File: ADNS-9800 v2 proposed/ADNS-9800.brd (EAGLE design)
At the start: 32.7 x 32.5 mm, 27 parts, among them Q1 TRANSISTOR_SC-75

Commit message: V2 Design
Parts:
- R1, R2, R4: value (none) -> 1.8K
- R3, R5, R6: value (none) -> 3.3K
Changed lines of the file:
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@@
 <element name="SJ1" library="SparkFun-Passives" package="SJ_2S-TRACE" value="SOLDERJUMPERTRACE" x="5.2" y="21.52" smashed="yes" rot="MR180"/>
 <element name="SJ4" library="SparkFun-Passives" package="SJ_2S-NO" value="SOLDERJUMPERNO" x="5.2" y="11.12" smashed="yes" rot="MR0"/>
-<element name="R1" library="SparkFun-Passives" package="0603-RES" value="" x="5.1933" y="21.479" smashed="yes">
+<element name="R1" library="SparkFun-Passives" package="0603-RES" value="1.8K" x="5.1933" y="21.479" smashed="yes">
 <attribute name="NAME" x="4.6243" y="22.081" size="1.016" layer="25" font="vector" ratio="10"/>
-<attribute name="VALUE" x="4.1773" y="20.336" size="0.4064" layer="27" font="vector"/>
 </element>
-<element name="R6" library="SparkFun-Passives" package="0603-RES" value="" x="5.2" y="11.12" smashed="yes">
+<element name="R6" library="SparkFun-Passives" package="0603-RES" value="3.3K" x="5.2" y="11.12" smashed="yes">
 <attribute name="NAME" x="4.311" y="11.802" size="1.016" layer="25" font="vector" ratio="10"/>
-<attribute name="VALUE" x="4.184" y="9.977" size="0.4064" layer="27" font="vector"/>
 </element>
-<element name="R2" library="SparkFun-Passives" package="0603-RES" value="" x="5.2" y="23.84" smashed="yes">
+<element name="R2" library="SparkFun-Passives" package="0603-RES" value="1.8K" x="5.2" y="23.84" smashed="yes">
 <attribute name="NAME" x="4.631" y="24.442" size="1.016" layer="25" font="vector" ratio="10"/>
-<attribute name="VALUE" x="4.184" y="22.697" size="0.4064" layer="27" font="vector"/>
 </element>
 <element name="SJ2" library="SparkFun-Passives" package="SJ_2S-NO" value="SOLDERJUMPERNO" x="5.2" y="13.52" smashed="yes" rot="MR0"/>
-<element name="R3" library="SparkFun-Passives" package="0603-RES" value="" x="5.2" y="13.52" smashed="yes">
+<element name="R3" library="SparkFun-Passives" package="0603-RES" value="3.3K" x="5.2" y="13.52" smashed="yes">
 <attribute name="NAME" x="4.311" y="14.122" size="1.016" layer="25" font="vector" ratio="10"/>
-<attribute name="VALUE" x="4.184" y="12.377" size="0.4064" layer="27" font="vector"/>
 </element>
 <element name="SJ3" library="SparkFun-Passives" package="SJ_2S-TRACE" value="SOLDERJUMPERTRACE" x="5.12" y="23.84" smashed="yes" rot="MR180"/>
-<element name="R4" library="SparkFun-Passives" package="0603-RES" value="" x="5.2" y="19.12" smashed="yes">
+<element name="R4" library="SparkFun-Passives" package="0603-RES" value="1.8K" x="5.2" y="19.12" smashed="yes">
 <attribute name="NAME" x="4.631" y="19.722" size="1.016" layer="25" font="vector" ratio="10"/>
-<attribute name="VALUE" x="4.184" y="17.977" size="0.4064" layer="27" font="vector"/>
 </element>
 <element name="SJ5" library="SparkFun-Passives" package="SJ_2S-NO" value="SOLDERJUMPERNO" x="5.2" y="8.72" smashed="yes" rot="MR0"/>
-<element name="R5" library="SparkFun-Passives" package="0603-RES" value="" x="5.2" y="8.72" smashed="yes">
+<element name="R5" library="SparkFun-Passives" package="0603-RES" value="3.3K" x="5.2" y="8.72" smashed="yes">
 <attribute name="NAME" x="4.311" y="9.402" size="1.016" layer="25" font="vector" ratio="10"/>
-<attribute name="VALUE" x="4.184" y="7.577" size="0.4064" layer="27" font="vector"/>
 </element>
 <element name="SJ6" library="SparkFun-Passives" package="SJ_2S-TRACE" value="SOLDERJUMPERTRACE" x="5.2" y="19.12" smashed="yes" rot="MR180"/>

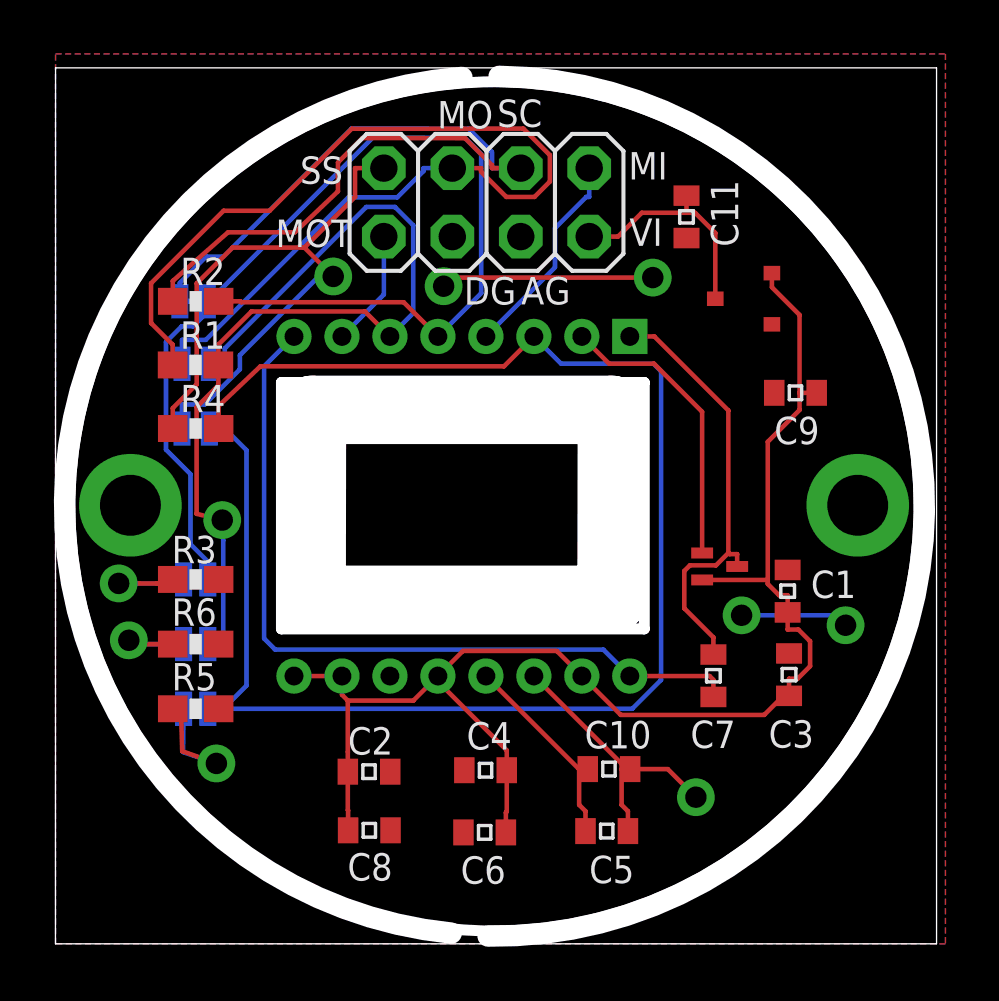
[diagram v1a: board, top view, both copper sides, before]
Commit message: v2 w/5V Support
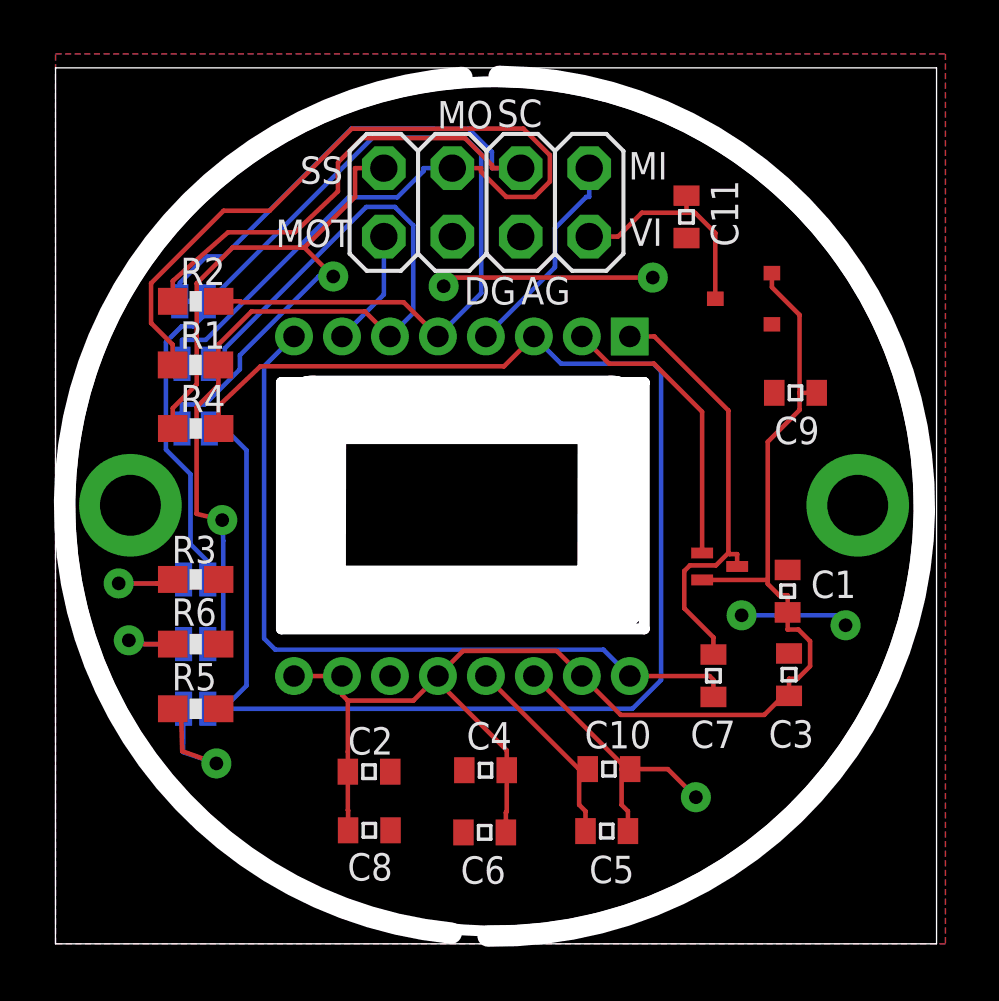
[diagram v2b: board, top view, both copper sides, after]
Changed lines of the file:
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@@
 <setting verticaltext="up"/>
 </settings>
-<grid distance="0.003125" unitdist="mic" unit="mm" style="lines" multiple="1" display="yes" altdistance="0.025" altunitdist="inch" altunit="inch"/>
+<grid distance="3.937008" unitdist="mil" unit="mil" style="lines" multiple="1" display="yes" altdistance="0.025" altunitdist="inch" altunit="inch"/>
 <layers>
 <layer number="1" name="Top" color="4" fill="1" visible="yes" active="yes"/>
@@
 <wire x1="6.1857" y1="15.7224" x2="6.2226" y2="14.9655" width="0.17" layer="16"/>
 <wire x1="6.2226" y1="14.9655" x2="6.2226" y2="11.12" width="0.17" layer="16"/>
-<via x="6.1857" y="15.7224" extent="1-16" drill="0.793796875" diameter="1.4034"/>
+<via x="6.1857" y="15.7224" extent="1-16" drill="0.508" diameter="1.016"/>
 </signal>
 <signal name="SS">
@@
 <contactref element="R5" pad="2"/>
 <contactref element="JP1" pad="4"/>
-<via x="25.456396875" y="12.189271875" extent="1-16" drill="0.793796875" diameter="1.4034"/>
-<via x="29.314465625" y="11.819475" extent="1-16" drill="0.793796875" diameter="1.4034"/>
+<via x="25.456396875" y="12.189271875" extent="1-16" drill="0.508" diameter="1.016"/>
+<via x="29.314465625" y="11.819475" extent="1-16" drill="0.508" diameter="1.016"/>
 <wire x1="29.314465625" y1="11.819475" x2="28.94466875" y2="12.189271875" width="0.17" layer="16"/>
 <wire x1="28.94466875" y1="12.189271875" x2="25.456396875" y2="12.189271875" width="0.17" layer="16"/>
+<wire x1="12.4201" y1="6.3867" x2="12.4081" y2="9.936" width="0" layer="19" extent="1-1"/>
 </signal>
 <signal name="N$5">
@@
 <wire x1="21.0038" y1="5.1554" x2="21.2389" y2="4.9203" width="0.17" layer="1"/>
 <wire x1="21.3218" y1="6.4828" x2="21.0038" y2="6.4828" width="0.17" layer="1"/>
-<via x="14.4" y="24.4" extent="1-16" drill="0.793796875" diameter="1.4034"/>
-<via x="22.16" y="24.72" extent="1-16" drill="0.793796875" diameter="1.4034"/>
+<via x="14.4" y="24.4" extent="1-16" drill="0.508" diameter="1.016"/>
+<via x="22.16" y="24.72" extent="1-16" drill="0.508" diameter="1.016"/>
 <wire x1="14.4" y1="24.4" x2="14.72" y2="24.72" width="0.17" layer="1"/>
 <wire x1="14.72" y1="24.72" x2="22.16" y2="24.72" width="0.17" layer="1"/>
-<via x="23.76" y="5.44" extent="1-16" drill="0.793796875" diameter="1.4034"/>
+<via x="23.76" y="5.44" extent="1-16" drill="0.508" diameter="1.016"/>
 <wire x1="23.76" y1="5.44" x2="22.7172" y2="6.4828" width="0.17" layer="1"/>
 <wire x1="22.7172" y1="6.4828" x2="21.3218" y2="6.4828" width="0.17" layer="1"/>
@@
 <wire x1="2.7193" y1="11.262" x2="3.2973" y2="11.12" width="0.17" layer="1"/>
 <wire x1="3.2973" y1="11.12" x2="4.35" y2="11.12" width="0.17" layer="1"/>
-<via x="2.7193" y="11.262" extent="1-16" drill="0.793796875" diameter="1.4034"/>
+<via x="2.7193" y="11.262" extent="1-16" drill="0.508" diameter="1.016"/>
 <wire x1="4.75" y1="11.12" x2="3.2973" y2="11.12" width="0.17" layer="16"/>
 <wire x1="3.2973" y1="11.12" x2="2.7193" y2="11.262" width="0.17" layer="16"/>
@@
 <wire x1="2.3434" y1="13.3728" x2="3.7579" y2="13.3728" width="0.17" layer="1"/>
 <wire x1="3.7579" y1="13.3728" x2="4.19" y2="13.4049" width="0.17" layer="1"/>
-<via x="2.3434" y="13.3728" extent="1-16" drill="0.793796875" diameter="1.4034"/>
+<via x="2.3434" y="13.3728" extent="1-16" drill="0.508" diameter="1.016"/>
 <wire x1="4.1774" y1="13.52" x2="4.1774" y2="13.3668" width="0.17" layer="16"/>
 <wire x1="4.1774" y1="13.3668" x2="2.3434" y2="13.3728" width="0.17" layer="16"/>
@@
 <wire x1="5.967890625" y1="6.6926375" x2="4.69973125" y2="7.14690625" width="0.17" layer="1"/>
 <wire x1="4.69973125" y1="7.14690625" x2="4.6649" y2="8.32" width="0.17" layer="1"/>
-<via x="5.967890625" y="6.6926375" extent="1-16" drill="0.793796875" diameter="1.4034"/>
+<via x="5.967890625" y="6.6926375" extent="1-16" drill="0.508" diameter="1.016"/>
 <wire x1="4.75" y1="8.72" x2="4.73259375" y2="7.114590625" width="0.17" layer="16"/>
 <wire x1="4.73259375" y1="7.114590625" x2="5.967890625" y2="6.6926375" width="0.17" layer="16"/>
@@
 <wire x1="12.1817" y1="28.7813" x2="11.1138" y2="28.7813" width="0.17" layer="1"/>
 <wire x1="4.692" y1="19.12" x2="4.692" y2="20.0101" width="0.17" layer="16"/>
-<via x="10.3045" y="24.7616" extent="1-16" drill="0.793796875" diameter="1.4034"/>
+<via x="10.3045" y="24.7616" extent="1-16" drill="0.508" diameter="1.016"/>
 <wire x1="4.35" y1="19.12" x2="4.35" y2="19.8751" width="0.17" layer="1"/>
 </signal>
